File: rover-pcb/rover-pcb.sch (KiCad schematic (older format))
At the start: 42 parts, among them J1 12V IN, J2 AVR-ISP-6, J3 Conn_01x04, J4 Conn_01x04, J5 Conn_01x04, J6 Conn_01x04, J7 HC-10, Q1 BSS138, Q2 BSS138, U1 L78L33_SOT89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

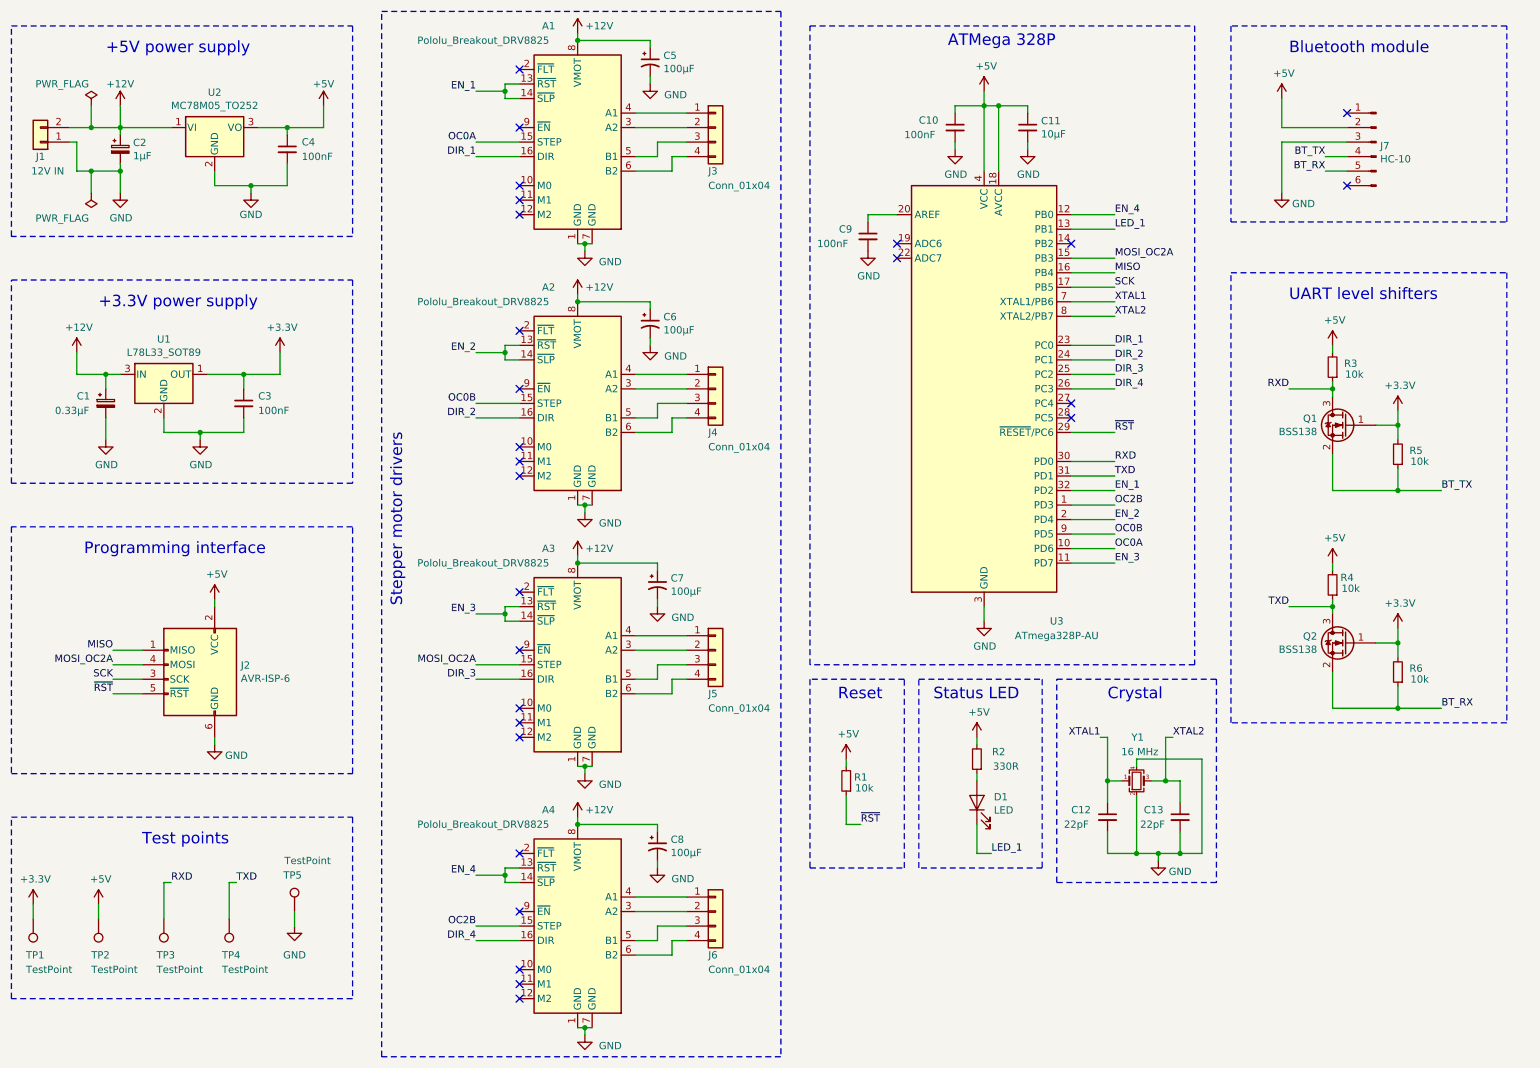
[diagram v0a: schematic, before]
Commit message: Adding Rover PCB layout.
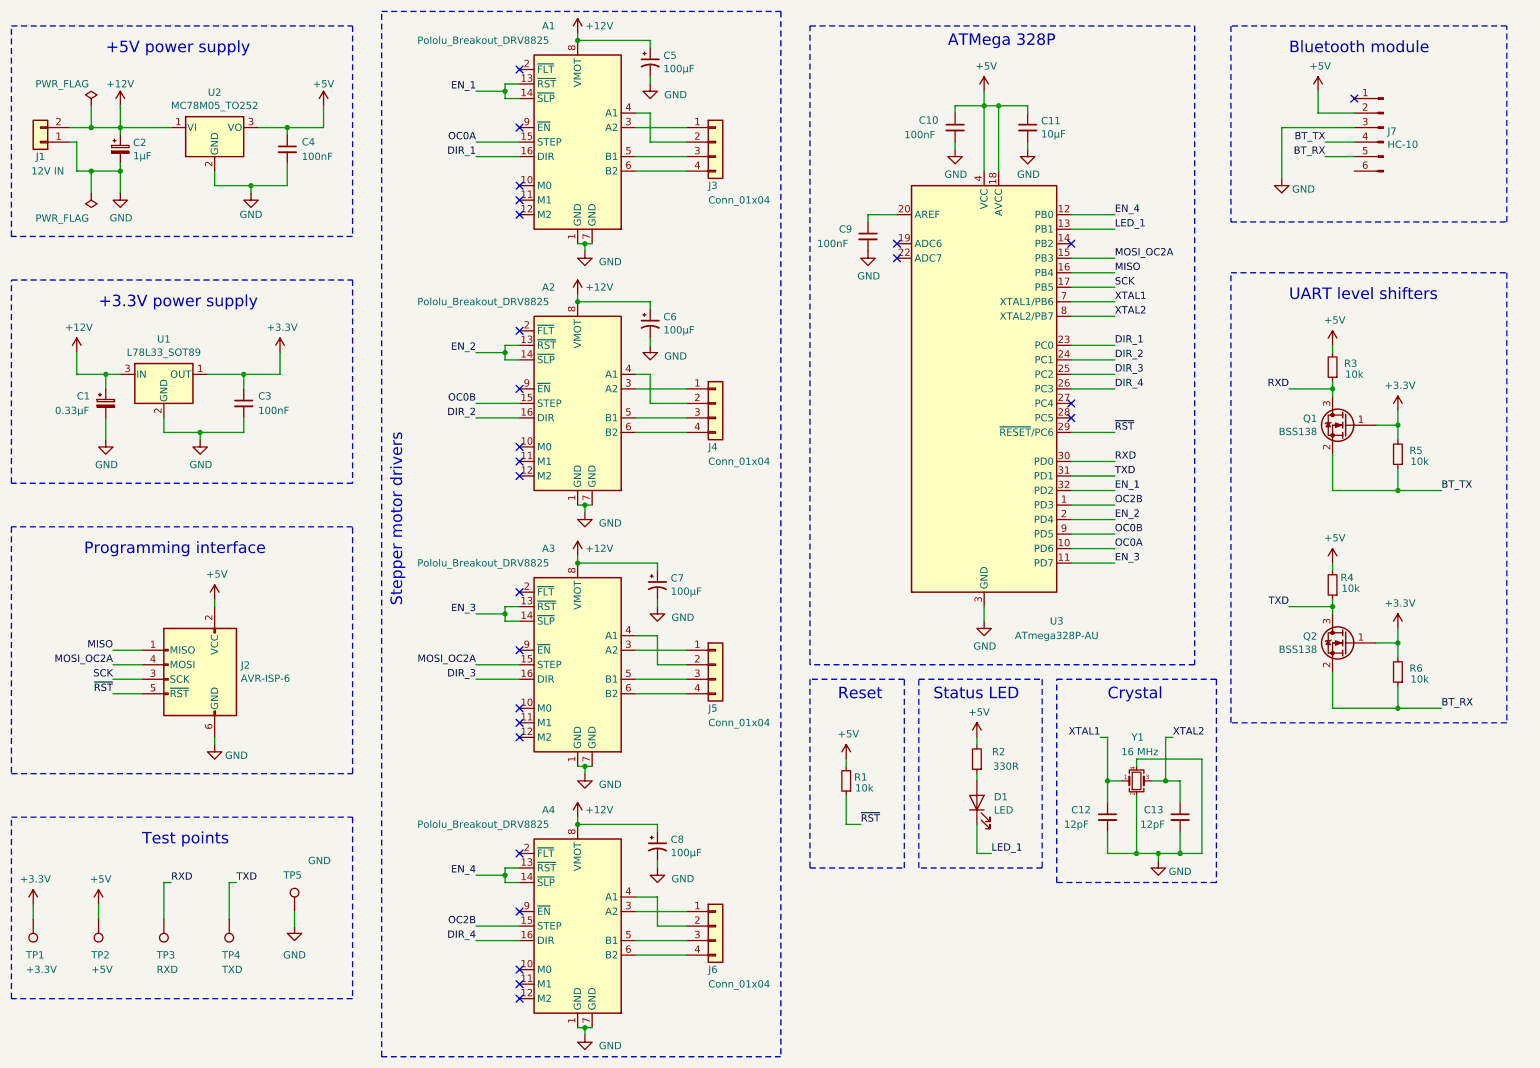
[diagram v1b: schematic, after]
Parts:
- C10, C3, C4, C9: footprint (none) -> Capacitor_SMD:C_0603_1608Metric_Pad1.05x0.95mm_HandSolder
- C12, C13: value 22pF -> 12pF; footprint (none) -> Capacitor_SMD:C_0603_1608Metric_Pad1.05x0.95mm_HandSolder
- C5, C6, C7, C8: footprint (none) -> Capacitor_SMD:CP_Elec_6.3x7.7
- D1: footprint (none) -> LED_SMD:LED_0805_2012Metric_Pad1.15x1.40mm_HandSolder
- J1: footprint (none) -> TerminalBlock_Phoenix:TerminalBlock_Phoenix_MKDS-1,5-2-5.08_1x02_P5.08mm_Horizontal
- J2: footprint (none) -> Connector_IDC:IDC-Header_2x03_P2.54mm_Vertical
- J3, J4, J5, J6: footprint (none) -> Connector_PinHeader_2.54mm:PinHeader_1x04_P2.54mm_Vertical
- J7: footprint (none) -> Connector_PinHeader_2.54mm:PinHeader_1x06_P2.54mm_Vertical
- R1, R2, R3, R4, R5, R6: footprint (none) -> Resistor_SMD:R_0603_1608Metric_Pad1.05x0.95mm_HandSolder
- TP1: value TestPoint -> +3.3V; footprint (none) -> TestPoint:TestPoint_THTPad_D2.0mm_Drill1.0mm
- TP2: value TestPoint -> +5V; footprint (none) -> TestPoint:TestPoint_THTPad_D2.0mm_Drill1.0mm
- TP3: value TestPoint -> RXD; footprint (none) -> TestPoint:TestPoint_THTPad_D2.0mm_Drill1.0mm
- TP4: value TestPoint -> TXD; footprint (none) -> TestPoint:TestPoint_THTPad_D2.0mm_Drill1.0mm
- TP5: value TestPoint -> GND; footprint (none) -> TestPoint:TestPoint_THTPad_D2.0mm_Drill1.0mm
- Y1: footprint (none) -> Crystal:Crystal_SMD_EuroQuartz_MJ-4Pin_5.0x3.2mm_HandSoldering
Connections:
- net at A1.3 (A2): now also J3.1 (Pin_1); no longer J3.2 (Pin_2)
- net at A1.4 (A1): now also J3.2 (Pin_2); no longer J3.1 (Pin_1)
- net at A2.3 (A2): now also J4.1 (Pin_1); no longer J4.2 (Pin_2)
- net at A2.4 (A1): now also J4.2 (Pin_2); no longer J4.1 (Pin_1)
- net at A3.3 (A2): now also J5.1 (Pin_1); no longer J5.2 (Pin_2)
- net at A3.4 (A1): now also J5.2 (Pin_2); no longer J5.1 (Pin_1)
- net at A4.3 (A2): now also J6.1 (Pin_1); no longer J6.2 (Pin_2)
- net at A4.4 (A1): now also J6.2 (Pin_2); no longer J6.1 (Pin_1)
- no-connect marks 27 -> 26
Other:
- moved on the sheet: J3, J4, J5, J6, J7

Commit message: Adding pads for external LEDs.
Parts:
- added J10: LED_3, rover-pcb:SolderWirePad_1x02_SMD_2x4mm, symbol Connector_Generic:Conn_01x02
- added J11: LED_4, rover-pcb:SolderWirePad_1x02_SMD_2x4mm, symbol Connector_Generic:Conn_01x02
- added J8: LED_1, rover-pcb:SolderWirePad_1x02_SMD_2x4mm, symbol Connector_Generic:Conn_01x02
- added J9: LED_2, rover-pcb:SolderWirePad_1x02_SMD_2x4mm, symbol Connector_Generic:Conn_01x02
- J3: value Conn_01x04 -> MOTOR_1
- J4: value Conn_01x04 -> MOTOR_2
- J5: value Conn_01x04 -> MOTOR_3
- J6: value Conn_01x04 -> MOTOR_4
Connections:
- net +12V: now also J10.1 (Pin_1), J11.1 (Pin_1), J8.1 (Pin_1), J9.1 (Pin_1)
- net GND: now also J10.2 (Pin_2), J11.2 (Pin_2), J8.2 (Pin_2), J9.2 (Pin_2)
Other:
- note added: "LED Lights"
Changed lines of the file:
@@
 Sheet 1 1
 Title "Mecanum Wheel Rover"
-Date "2019-09-30"
+Date "2019-10-01"
 Rev "1"
 Comp "Emil Jaregran"
@@
 P 5450 1400
 F 0 "J3" H 5400 1100 50  0000 L CNN
-F 1 "Conn_01x04" H 5400 1000 50  0000 L CNN
+F 1 "MOTOR_1" H 5400 1000 50  0000 L CNN
 F 2 "Connector_PinHeader_2.54mm:PinHeader_1x04_P2.54mm_Vertical" H 5450 1400 50  0001 C CNN
 F 3 "~" H 5450 1400 50  0001 C CNN
@@
 P 5450 3200
 F 0 "J4" H 5400 2900 50  0000 L CNN
-F 1 "Conn_01x04" H 5400 2800 50  0000 L CNN
+F 1 "MOTOR_2" H 5400 2800 50  0000 L CNN
 F 2 "Connector_PinHeader_2.54mm:PinHeader_1x04_P2.54mm_Vertical" H 5450 3200 50  0001 C CNN
 F 3 "~" H 5450 3200 50  0001 C CNN
@@
 P 5450 5000
 F 0 "J5" H 5400 4700 50  0000 L CNN
-F 1 "Conn_01x04" H 5400 4600 50  0000 L CNN
+F 1 "MOTOR_3" H 5400 4600 50  0000 L CNN
 F 2 "Connector_PinHeader_2.54mm:PinHeader_1x04_P2.54mm_Vertical" H 5450 5000 50  0001 C CNN
 F 3 "~" H 5450 5000 50  0001 C CNN
@@
 P 5450 6800
 F 0 "J6" H 5400 6500 50  0000 L CNN
-F 1 "Conn_01x04" H 5400 6400 50  0000 L CNN
+F 1 "MOTOR_4" H 5400 6400 50  0000 L CNN
 F 2 "Connector_PinHeader_2.54mm:PinHeader_1x04_P2.54mm_Vertical" H 5450 6800 50  0001 C CNN
 F 3 "~" H 5450 6800 50  0001 C CNN
@@
 Wire Wire Line
 	9650 1500 9850 1500
+$Comp
+L power:+12V #PWR041
+U 1 1 5D958AE7
+P 9375 5925
+F 0 "#PWR041" H 9375 5775 50  0001 C CNN
+F 1 "+12V" H 9375 6075 50  0000 C CNN
+F 2 "" H 9375 5925 50  0001 C CNN
+F 3 "" H 9375 5925 50  0001 C CNN
+	1    9375 5925
+	1    0    0    -1
+$EndComp
+$Comp
+L power:GND #PWR040
+U 1 1 5D95CD16
+P 9125 6225
+F 0 "#PWR040" H 9125 5975 50  0001 C CNN
+F 1 "GND" H 9125 6025 50  0000 C CNN
+F 2 "" H 9125 6225 50  0001 C CNN
+F 3 "" H 9125 6225 50  0001 C CNN
+	1    9125 6225
+	1    0    0    -1
+$EndComp
+$Comp
+L Connector_Generic:Conn_01x02 J8
+U 1 1 5D95DA1E
+P 9375 6150
+F 0 "J8" V 9475 6140 50  0000 L CNN
+F 1 "LED_1" V 9575 6000 50  0000 L CNN
+F 2 "rover-pcb:SolderWirePad_1x02_SMD_2x4mm" H 9375 6150 50  0001 C CNN
+F 3 "~" H 9375 6150 50  0001 C CNN
+	1    9375 6150
+	0    1    1    0
+$EndComp
+Wire Wire Line
+	9275 5950 9125 5950
+$Comp
+L power:+12V #PWR043
+U 1 1 5D9B7D79
+P 9875 5925
+F 0 "#PWR043" H 9875 5775 50  0001 C CNN
+F 1 "+12V" H 9875 6075 50  0000 C CNN
+F 2 "" H 9875 5925 50  0001 C CNN
+F 3 "" H 9875 5925 50  0001 C CNN
+	1    9875 5925
+	1    0    0    -1
+$EndComp
+$Comp
+L power:GND #PWR042
+U 1 1 5D9B7D83
+P 9625 6225
+F 0 "#PWR042" H 9625 5975 50  0001 C CNN
+F 1 "GND" H 9625 6025 50  0000 C CNN
+F 2 "" H 9625 6225 50  0001 C CNN
+F 3 "" H 9625 6225 50  0001 C CNN
+	1    9625 6225
+	1    0    0    -1
+$EndComp
+$Comp
+L Connector_Generic:Conn_01x02 J9
+U 1 1 5D9B7D8D
+P 9875 6150
+F 0 "J9" V 9975 6125 50  0000 L CNN
+F 1 "LED_2" V 10075 6000 50  0000 L CNN
+F 2 "rover-pcb:SolderWirePad_1x02_SMD_2x4mm" H 9875 6150 50  0001 C CNN
+F 3 "~" H 9875 6150 50  0001 C CNN
+	1    9875 6150
+	0    1    1    0
+$EndComp
+Wire Wire Line
+	9775 5950 9625 5950
+$Comp
+L power:+12V #PWR045
+U 1 1 5D9C91A9
+P 10375 5925
+F 0 "#PWR045" H 10375 5775 50  0001 C CNN
+F 1 "+12V" H 10375 6075 50  0000 C CNN
+F 2 "" H 10375 5925 50  0001 C CNN
+F 3 "" H 10375 5925 50  0001 C CNN
+	1    10375 5925
+	1    0    0    -1
+$EndComp
+$Comp
+L power:GND #PWR044
+U 1 1 5D9C91B3
+P 10125 6225
+F 0 "#PWR044" H 10125 5975 50  0001 C CNN
+F 1 "GND" H 10125 6025 50  0000 C CNN
+F 2 "" H 10125 6225 50  0001 C CNN
+F 3 "" H 10125 6225 50  0001 C CNN
+	1    10125 6225
+	1    0    0    -1
+$EndComp
+$Comp
+L Connector_Generic:Conn_01x02 J10
+U 1 1 5D9C91BD
+P 10375 6150
+F 0 "J10" V 10475 6125 50  0000 L CNN
+F 1 "LED_3" V 10575 6000 50  0000 L CNN
+F 2 "rover-pcb:SolderWirePad_1x02_SMD_2x4mm" H 10375 6150 50  0001 C CNN
+F 3 "~" H 10375 6150 50  0001 C CNN
+	1    10375 6150
+	0    1    1    0
+$EndComp
+Wire Wire Line
+	10275 5950 10125 5950
+Wire Wire Line
+	9125 6225 9125 5950
+Wire Wire Line
+	9375 5950 9375 5925
+Wire Wire Line
+	9625 6225 9625 5950
+Wire Wire Line
+	9875 5950 9875 5925
+Wire Wire Line
+	10125 6225 10125 5950
+Wire Wire Line
+	10375 5950 10375 5925
+$Comp
+L power:+12V #PWR047
+U 1 1 5DB01B81
+P 10875 5925
+F 0 "#PWR047" H 10875 5775 50  0001 C CNN
+F 1 "+12V" H 10875 6075 50  0000 C CNN
+F 2 "" H 10875 5925 50  0001 C CNN
+F 3 "" H 10875 5925 50  0001 C CNN
+	1    10875 5925
+	1    0    0    -1
+$EndComp
+$Comp
+L power:GND #PWR046
+U 1 1 5DB01B8B
+P 10625 6225
+F 0 "#PWR046" H 10625 5975 50  0001 C CNN
+F 1 "GND" H 10625 6025 50  0000 C CNN
+F 2 "" H 10625 6225 50  0001 C CNN
+F 3 "" H 10625 6225 50  0001 C CNN
+	1    10625 6225
+	1    0    0    -1
+$EndComp
+$Comp
+L Connector_Generic:Conn_01x02 J11
+U 1 1 5DB01B95
+P 10875 6150
+F 0 "J11" V 10975 6125 50  0000 L CNN
+F 1 "LED_4" V 11075 6000 50  0000 L CNN
+F 2 "rover-pcb:SolderWirePad_1x02_SMD_2x4mm" H 10875 6150 50  0001 C CNN
+F 3 "~" H 10875 6150 50  0001 C CNN
+	1    10875 6150
+	0    1    1    0
+$EndComp
+Wire Wire Line
+	10775 5950 10625 5950
+Wire Wire Line
+	10625 6225 10625 5950
+Wire Wire Line
+	10875 5950 10875 5925
+Text Notes 9675 5650 0    79   ~ 0
+LED Lights
+Wire Notes Line
+	9000 6500 9000 5500
+Wire Notes Line
+	9000 5500 11050 5500
+Wire Notes Line
+	11050 5500 11050 6500
+Wire Notes Line
+	11050 6500 9000 6500
 $EndSCHEMATC
